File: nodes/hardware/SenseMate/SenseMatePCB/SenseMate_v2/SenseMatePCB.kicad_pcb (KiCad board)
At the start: 2 copper layers, 32.8 x 59.8 mm, 20 parts, among them J1 Conn_01x04, J2 Conn_01x12_Pin, J3 Conn_Coaxial, J4 Conn_01x06_Pin, J5 Conn_01x06_Pin, J6 Conn_01x02_Pin, M1 Motor_DC, Q3 SS8050, Q4 SS8050, SW5 SW_DPDT_x2, U1 XIAO-nRF52840-Plus-SMD, U2 RFM95W-868S2

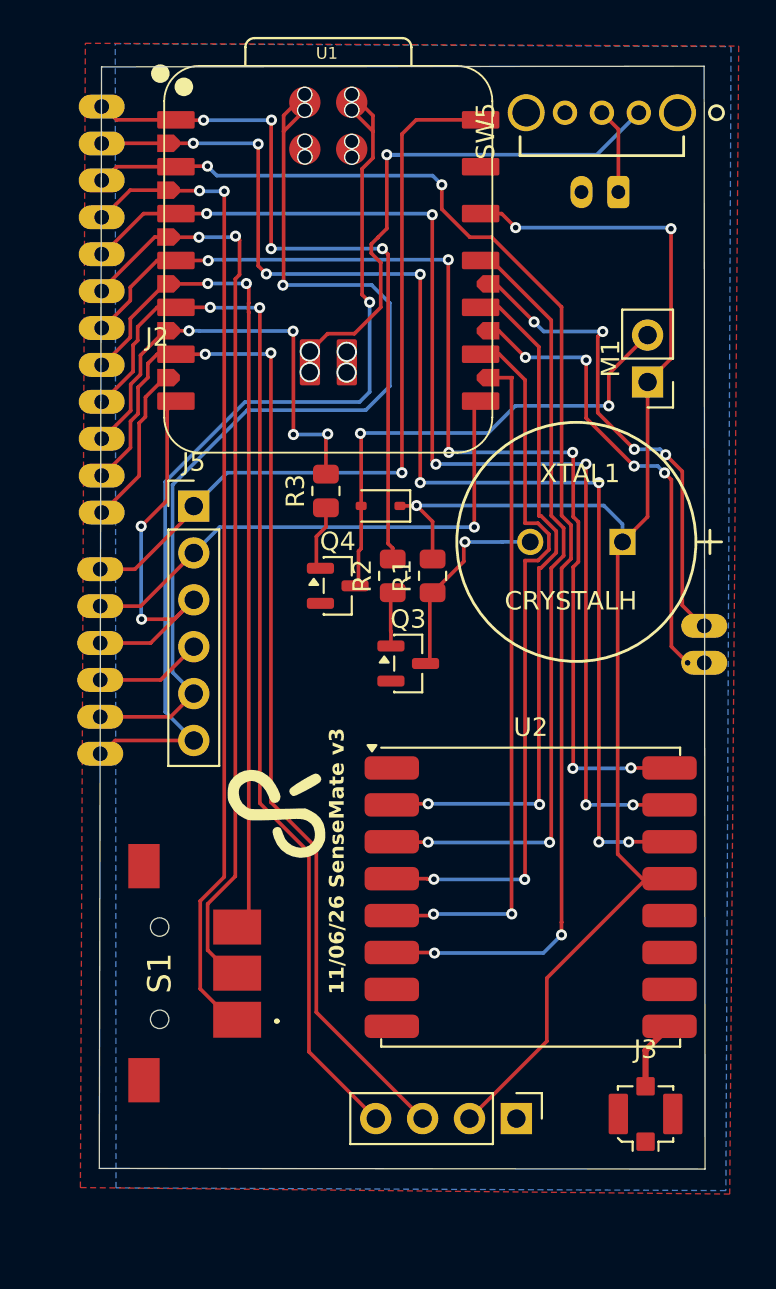
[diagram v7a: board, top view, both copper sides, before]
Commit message: added mounting hole
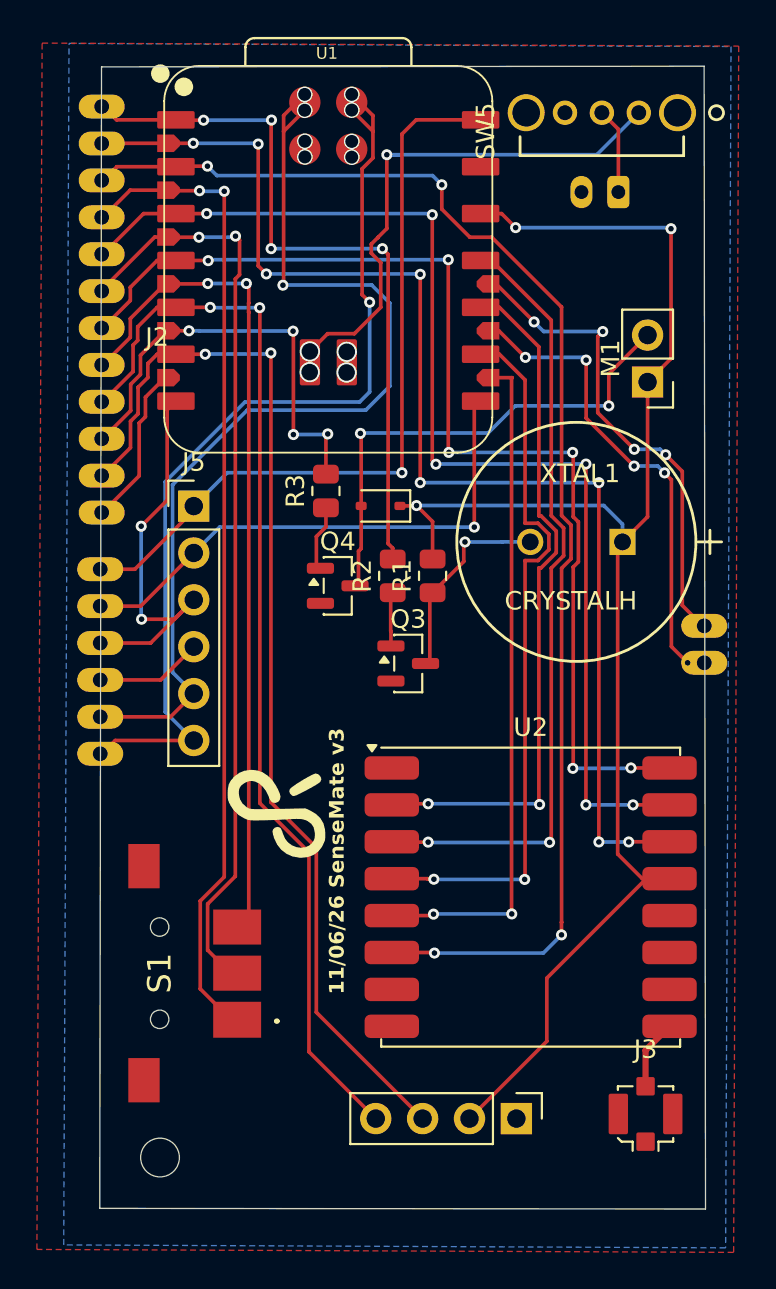
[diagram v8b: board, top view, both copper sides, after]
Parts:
- added REF**: MountingHole_2.1mm, MountingHole:MountingHole_2.1mm, F.Cu at (92.2, 86.1)
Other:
- board size 32.8 x 59.8 mm -> 32.8 x 61.9 mm
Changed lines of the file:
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@@
 		)
 	)
+	(footprint "MountingHole:MountingHole_2.1mm"
+		(layer "F.Cu")
+		(at 92.19 86.11)
+		(descr "Mounting Hole 2.1mm, no annular, generated by kicad-footprint-generator mountinghole.py")
+		(tags "mountinghole")
+		(property "Reference" "REF**"
+			(at 0 -3.05 0)
+			(layer "F.SilkS")
+			(hide yes)
+			(effects
+				(font
+					(size 1 1)
+					(thickness 0.15)
+				)
+			)
+		)
+		(property "Value" "MountingHole_2.1mm"
+			(at 1.11 3.01 180)
+			(layer "F.Fab")
+			(effects
+				(font
+					(size 1 1)
+					(thickness 0.15)
+				)
+			)
+		)
+		(property "Datasheet" ""
+			(at 0 0 0)
+			(layer "F.Fab")
+			(hide yes)
+			(effects
+				(font
+					(size 1.27 1.27)
+					(thickness 0.15)
+				)
+			)
+		)
+		(property "Description" ""
+			(at 0 0 0)
+			(layer "F.Fab")
+			(hide yes)
+			(effects
+				(font
+					(size 1.27 1.27)
+					(thickness 0.15)
+				)
+			)
+		)
+		(attr exclude_from_pos_files exclude_from_bom)
+		(duplicate_pad_numbers_are_jumpers no)
+		(fp_circle
+			(center 0 0)
+			(end 2.1 0)
+			(stroke
+				(width 0.15)
+				(type solid)
+			)
+			(fill no)
+			(layer "Cmts.User")
+		)
+		(fp_circle
+			(center 0 0)
+			(end 2.35 0)
+			(stroke
+				(width 0.05)
+				(type solid)
+			)
+			(fill no)
+			(layer "F.CrtYd")
+		)
+		(pad "" np_thru_hole circle
+			(at 0 0)
+			(size 2.1 2.1)
+			(drill 2.1)
+			(layers "*.Cu" "*.Mask")
+		)
+		(embedded_fonts no)
+	)
 	(footprint "SenseMateLibrary:Castellated_1x6_2.00mm"
 		(layer "F.Cu")
@@
 	)
 	(gr_line
-		(start 88.9 86.7)
+		(start 88.925 88.866)
 		(end 89.02 27.01)
 		(stroke
@@
 	)
 	(gr_line
-		(start 88.9 86.7)
-		(end 121.725 86.734)
+		(start 88.925 88.866)
+		(end 121.75 88.9)
 		(stroke
 			(width 0.058206)
@@
 	)
 	(gr_line
-		(start 121.725 86.734)
+		(start 121.75 88.9)
 		(end 121.674069 26.973129)
 		(stroke
@@
 		(polygon
 			(pts
-				(xy 88.143392 25.731416) (xy 123.548253 25.884382) (xy 123.061007 88.090135) (xy 87.875493 87.738201)
+				(xy 85.801231 25.721297) (xy 123.548253 25.884382) (xy 123.272613 91.249848) (xy 85.518804 91.090644)
 			)
 		)
@@
 		(polygon
 			(pts
-				(xy 89.764833 25.750953) (xy 123.131892 25.908151) (xy 122.853068 87.901808) (xy 89.803875 87.753165)
+				(xy 87.259504 25.73915) (xy 123.131892 25.908151) (xy 122.839114 91.004296) (xy 86.970896 90.845297)
 			)
 		)
